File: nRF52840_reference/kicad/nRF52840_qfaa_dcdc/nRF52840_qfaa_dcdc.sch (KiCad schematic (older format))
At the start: 33 parts, among them J1 CONN_COAXIAL, U1 nRF52840, X1 XTAL_32MHZ, X2 XTAL_32KHZ

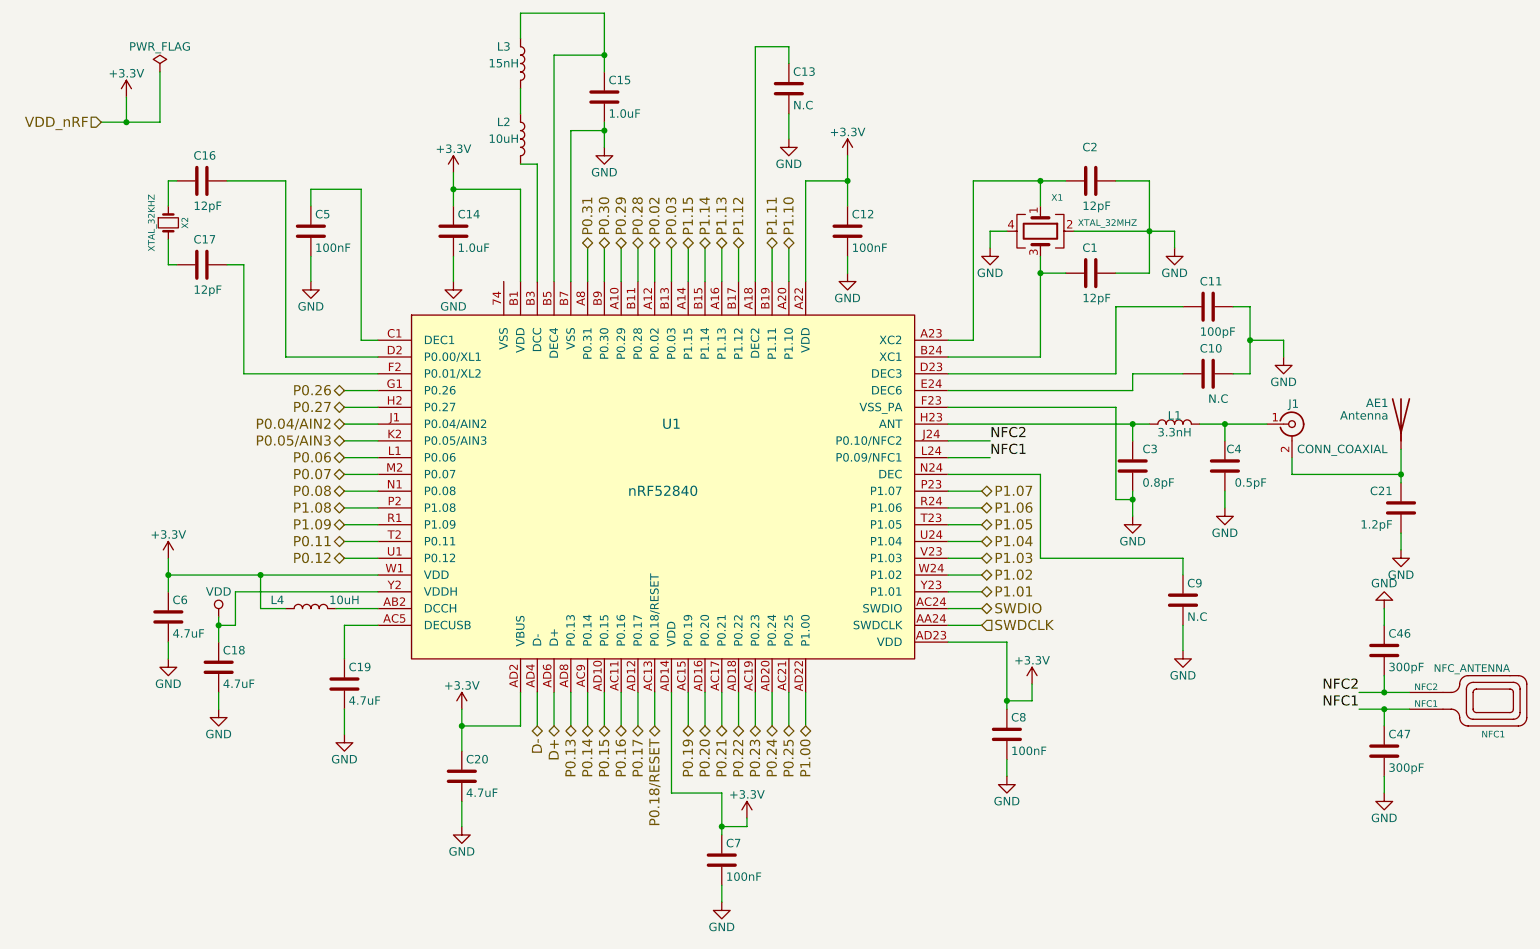
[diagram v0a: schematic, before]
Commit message: Update KiCAD Project nRF52840_qfaa_dcdc
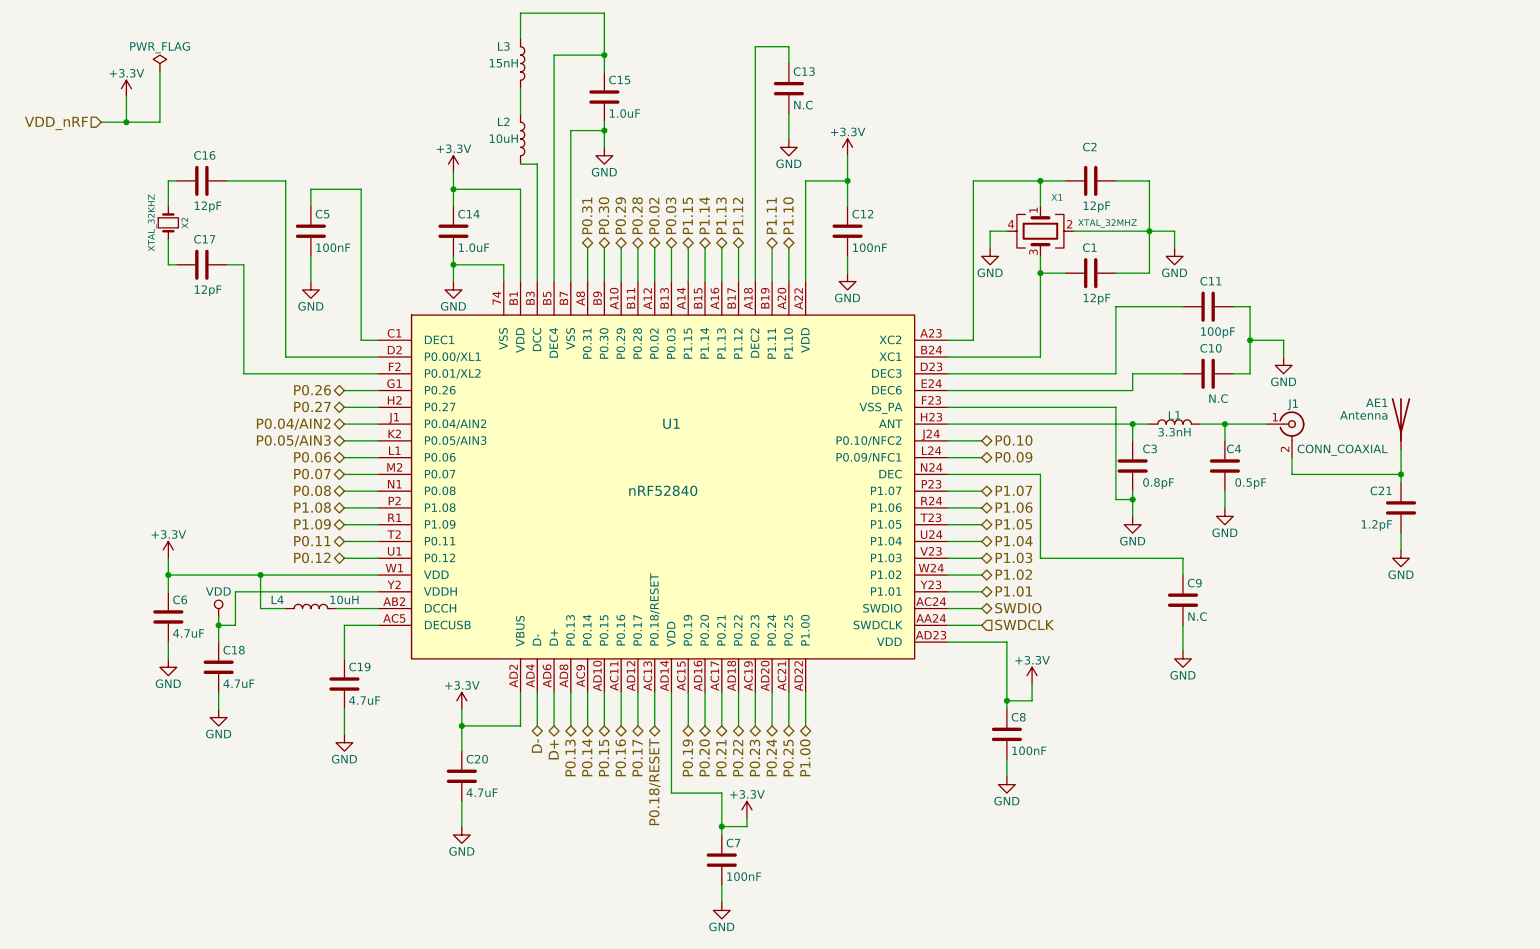
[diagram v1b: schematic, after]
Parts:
- removed C46, C47: 300pF, Nordic_misc:C_0402, symbol C
- removed NFC1: NFC_ANTENNA, Nordic_misc:Nordic_misc-NFC_ANT, symbol NFC_ANTENNA
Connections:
- net GND: now also U1.74 (VSS)
- net NFC1 renamed P0.09
- net NFC2 renamed P0.10
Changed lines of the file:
@@
 	2750 4200 2550 4200
 Wire Wire Line
-	6400 3500 6150 3500
-Wire Wire Line
-	6150 3600 6400 3600
+	6350 3500 6150 3500
+Wire Wire Line
+	6150 3600 6350 3600
 Wire Wire Line
 	6350 3800 6150 3800
@@
 Wire Wire Line
 	6700 4200 6700 3700
-$Comp
-L NFC_ANTENNA NFC1
-U 1 1 5984E4A9
-P 9400 5200
-F 0 "NFC1" H 9400 5150 39  0000 C CNN
-F 1 "NFC_ANTENNA" H 9500 5570 45  0000 R TNN
-F 2 "Nordic_misc:Nordic_misc-NFC_ANT" H 9430 5350 20  0001 C CNN
-F 3 "" H 9400 5200 60  0001 C CNN
-	1    9400 5200
-	1    0    0    -1
-$EndComp
-Text Label 6400 3500 0    60   ~ 0
-NFC2
-Text Label 6400 3600 0    60   ~ 0
-NFC1
-Wire Wire Line
-	8600 5000 8900 5000
-Wire Wire Line
-	8600 5100 8900 5100
-$Comp
-L C C47
-U 1 1 5984F3D3
-P 8750 5350
-F 0 "C47" H 8775 5450 50  0000 L CNN
-F 1 "300pF" H 8775 5250 50  0000 L CNN
-F 2 "Nordic_misc:C_0402" H 8788 5200 50  0001 C CNN
-F 3 "" H 8750 5350 50  0001 C CNN
-	1    8750 5350
-	1    0    0    -1
-$EndComp
-$Comp
-L C C46
-U 1 1 5984F45C
-P 8750 4750
-F 0 "C46" H 8775 4850 50  0000 L CNN
-F 1 "300pF" H 8775 4650 50  0000 L CNN
-F 2 "Nordic_misc:C_0402" H 8788 4600 50  0001 C CNN
-F 3 "" H 8750 4750 50  0001 C CNN
-	1    8750 4750
-	1    0    0    -1
-$EndComp
-Wire Wire Line
-	8750 5000 8750 4900
-Wire Wire Line
-	8750 5200 8750 5100
-$Comp
-L GND #PWR028
-U 1 1 5984F7AF
-P 8750 5600
-F 0 "#PWR028" H 8750 5350 50  0001 C CNN
-F 1 "GND" H 8750 5450 50  0000 C CNN
-F 2 "" H 8750 5600 50  0001 C CNN
-F 3 "" H 8750 5600 50  0001 C CNN
-	1    8750 5600
-	1    0    0    -1
-$EndComp
-Wire Wire Line
-	8750 5600 8750 5500
-$Comp
-L GND #PWR029
-U 1 1 5984FAF0
-P 8750 4500
-F 0 "#PWR029" H 8750 4250 50  0001 C CNN
-F 1 "GND" H 8750 4350 50  0000 C CNN
-F 2 "" H 8750 4500 50  0001 C CNN
-F 3 "" H 8750 4500 50  0001 C CNN
-	1    8750 4500
-	-1   0    0    1
-$EndComp
-Wire Wire Line
-	8750 4600 8750 4500
-Connection ~ 8750 5000
-Connection ~ 8750 5100
-Text Label 8600 5100 2    60   ~ 0
-NFC1
-Text Label 8600 5000 2    60   ~ 0
-NFC2
+Text HLabel 6350 3600 2    60   BiDi ~ 0
+P0.09
+Text HLabel 6350 3500 2    60   BiDi ~ 0
+P0.10
+Wire Wire Line
+	3500 2550 3500 2450
+Wire Wire Line
+	3500 2450 3200 2450
+Connection ~ 3200 2450
 $EndSCHEMATC
